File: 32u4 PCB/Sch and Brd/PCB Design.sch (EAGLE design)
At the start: 56 parts, among them J1 AVR_SPI_PROG_3X2PTH, J2 AMP FCI 10103594-0001LF, Q1 16MHz, U1 ATMEGA32U4-AU

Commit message: Started routinng
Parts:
- removed CONT: 50k, pot:TRIM_EU-S64W
- added I2C: (no value), pinhead:PINHD-1X4
- added R13: 220, resistor:R-EU_M0805
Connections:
- net +12V: no longer X1-2.KL
- net +5V: now also I2C.2; no longer CONT.E
- net GND: now also I2C.1, R13.1; no longer CONT.A, X1-1.KL
- net N$6: now also R13.2; no longer CONT.S
- net PD0/SCL: now also I2C.3
- net PD1/SDA: now also I2C.4
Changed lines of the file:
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@@
 <setting verticaltext="up"/>
 </settings>
-<grid distance="0.05" unitdist="inch" unit="inch" style="lines" multiple="1" display="no" altdistance="0.005" altunitdist="inch" altunit="inch"/>
+<grid distance="0.1" unitdist="inch" unit="inch" style="lines" multiple="1" display="no" altdistance="0.01" altunitdist="inch" altunit="inch"/>
 <layers>
 <layer number="1" name="Top" color="4" fill="1" visible="no" active="no"/>
@@
 </part>
 <part name="GND22" library="supply1" deviceset="GND" device=""/>
-<part name="CONT" library="pot" library_urn="urn:adsk.eagle:library:331" deviceset="TRIM_EU-" device="S64W" value="50k">
-<attribute name="MF" value=""/>
-<attribute name="MPN" value=""/>
-<attribute name="OC_FARNELL" value="unknown"/>
-</part>
-<part name="P+13" library="supply1" deviceset="+5V" device=""/>
-<part name="GND19" library="supply1" deviceset="GND" device=""/>
 <part name="P+12" library="supply1" deviceset="+5V" device=""/>
 <part name="LCD1" library="SparkFun-Displays" deviceset="LCD-16X2" device="NOSILK">
@@
 <part name="X1" library="con-ptr500" library_urn="urn:adsk.eagle:library:181" deviceset="AK500/2-H" device="" package3d_urn="urn:adsk.eagle:package:9901/1"/>
 <part name="MPU6040" library="pinhead" library_urn="urn:adsk.eagle:library:325" deviceset="PINHD-1X8" device="" package3d_urn="urn:adsk.eagle:package:22409/2"/>
+<part name="R13" library="resistor" library_urn="urn:adsk.eagle:library:348" deviceset="R-EU_" device="M0805" value="220">
+<attribute name="MF" value=""/>
+<attribute name="MPN" value=""/>
+<attribute name="OC_FARNELL" value="unknown"/>
+</part>
+<part name="GND3" library="supply1" deviceset="GND" device=""/>
+<part name="I2C" library="pinhead" library_urn="urn:adsk.eagle:library:325" deviceset="PINHD-1X4" device="" package3d_urn="urn:adsk.eagle:package:22407/2"/>
 </parts>
 <sheets>
@@
 <instance part="X1" gate="-2" x="3.81" y="144.78" rot="R180"/>
 <instance part="MPU6040" gate="A" x="139.7" y="-114.3"/>
+<instance part="I2C" gate="A" x="160.02" y="-66.04"/>
 </instances>
 <busses>
@@
 <wire x1="137.16" y1="-104.14" x2="132.08" y2="-104.14" width="0.1524" layer="91"/>
 <label x="132.08" y="-104.14" size="1.016" layer="95" rot="R180" xref="yes"/>
+</segment>
+<segment>
+<pinref part="I2C" gate="A" pin="2"/>
+<wire x1="157.48" y1="-63.5" x2="152.4" y2="-63.5" width="0.1524" layer="91"/>
+<label x="152.4" y="-63.5" size="1.016" layer="95" rot="R180" xref="yes"/>
 </segment>
 </net>
@@
 <wire x1="-12.7" y1="137.16" x2="-17.78" y2="137.16" width="0.1524" layer="91"/>
 <junction x="-17.78" y="137.16"/>
-<wire x1="-12.7" y1="137.16" x2="-1.27" y2="137.16" width="0.1524" layer="91"/>
-<junction x="-12.7" y="137.16"/>
-<pinref part="X1" gate="-1" pin="KL"/>
-<wire x1="-1.27" y1="138.43" x2="-1.27" y2="137.16" width="0.1524" layer="91"/>
 </segment>
 <segment>
@@
 <label x="132.08" y="-106.68" size="1.016" layer="95" rot="R180" xref="yes"/>
 </segment>
+<segment>
+<pinref part="I2C" gate="A" pin="1"/>
+<wire x1="157.48" y1="-60.96" x2="152.4" y2="-60.96" width="0.1524" layer="91"/>
+<label x="152.4" y="-60.96" size="1.016" layer="95" rot="R180" xref="yes"/>
+</segment>
 </net>
 <net name="PD1/SDA" class="0">
@@
 <wire x1="137.16" y1="-111.76" x2="132.08" y2="-111.76" width="0.1524" layer="91"/>
 <label x="132.08" y="-111.76" size="1.016" layer="95" rot="R180" xref="yes"/>
+</segment>
+<segment>
+<pinref part="I2C" gate="A" pin="4"/>
+<wire x1="157.48" y1="-68.58" x2="152.4" y2="-68.58" width="0.1524" layer="91"/>
+<label x="152.4" y="-68.58" size="1.016" layer="95" rot="R180" xref="yes"/>
 </segment>
 </net>
@@
 <junction x="-22.86" y="144.78"/>
 <pinref part="C1" gate="G$1" pin="+"/>
-<junction x="-12.7" y="144.78"/>
-<pinref part="X1" gate="-2" pin="KL"/>
-<wire x1="-1.27" y1="144.78" x2="-12.7" y2="144.78" width="0.1524" layer="91"/>
 </segment>
 </net>
@@
 <wire x1="137.16" y1="-109.22" x2="132.08" y2="-109.22" width="0.1524" layer="91"/>
 <label x="132.08" y="-109.22" size="1.016" layer="95" rot="R180" xref="yes"/>
+</segment>
+<segment>
+<pinref part="I2C" gate="A" pin="3"/>
+<wire x1="157.48" y1="-66.04" x2="152.4" y2="-66.04" width="0.1524" layer="91"/>
+<label x="152.4" y="-66.04" size="1.016" layer="95" rot="R180" xref="yes"/>
 </segment>
 </net>
@@
 </instance>
 <instance part="GND22" gate="1" x="22.86" y="15.24"/>
-<instance part="CONT" gate="1" x="-8.885290625" y="64.38225" smashed="yes">
-<attribute name="NAME" x="-14.854290625" y="60.57225" size="1.778" layer="95" rot="R90"/>
-<attribute name="VALUE" x="-12.695290625" y="60.57225" size="1.778" layer="96" rot="R90"/>
-<attribute name="OC_FARNELL" x="-8.885290625" y="64.38225" size="1.778" layer="96" display="off"/>
-<attribute name="MF" x="-8.885290625" y="64.38225" size="1.778" layer="96" display="off"/>
-<attribute name="MPN" x="-8.885290625" y="64.38225" size="1.778" layer="96" display="off"/>
-</instance>
-<instance part="P+13" gate="1" x="-10.16" y="73.66" smashed="yes">
-<attribute name="VALUE" x="-7.62" y="76.2" size="1.778" layer="96" rot="R180"/>
-</instance>
-<instance part="GND19" gate="1" x="-10.16" y="55.88"/>
 <instance part="P+12" gate="1" x="-5.08" y="33.02" smashed="yes" rot="R90">
 <attribute name="VALUE" x="0" y="35.56" size="1.778" layer="96" rot="R180"/>
@@
 <attribute name="MPN" x="35.56" y="48.26" size="1.778" layer="96" display="off"/>
 </instance>
+<instance part="R13" gate="G$1" x="-2.54" y="58.42" rot="R90">
+<attribute name="OC_FARNELL" x="-2.54" y="58.42" size="1.778" layer="96" display="off"/>
+<attribute name="MF" x="-2.54" y="58.42" size="1.778" layer="96" display="off"/>
+<attribute name="MPN" x="-2.54" y="58.42" size="1.778" layer="96" display="off"/>
+</instance>
+<instance part="GND3" gate="1" x="-2.54" y="48.26"/>
 </instances>
 <busses>
@@
 </segment>
 <segment>
-<pinref part="GND19" gate="1" pin="GND"/>
-<pinref part="CONT" gate="1" pin="A"/>
-<wire x1="-10.16" y1="58.42" x2="-8.885290625" y2="58.42" width="0.1524" layer="91"/>
-<wire x1="-8.885290625" y1="58.42" x2="-8.885290625" y2="59.30225" width="0.1524" layer="91"/>
+<pinref part="R13" gate="G$1" pin="1"/>
+<pinref part="GND3" gate="1" pin="GND"/>
+<wire x1="-2.54" y1="50.8" x2="-2.54" y2="53.34" width="0.1524" layer="91"/>
 </segment>
 </net>
@@
 <segment>
 <wire x1="25.4" y1="63.5" x2="-2.54" y2="63.5" width="0.1524" layer="91"/>
-<pinref part="CONT" gate="1" pin="S"/>
-<wire x1="-3.805290625" y1="64.38225" x2="-2.54" y2="64.38225" width="0.1524" layer="91"/>
-<wire x1="-2.54" y1="64.38225" x2="-2.54" y2="63.5" width="0.1524" layer="91"/>
 <pinref part="LCD1" gate="G$1" pin="VO"/>
+<pinref part="R13" gate="G$1" pin="2"/>
+<junction x="-2.54" y="63.5"/>
 </segment>
 </net>
@@
 </segment>
 <segment>
-<pinref part="P+13" gate="1" pin="+5V"/>
-<pinref part="CONT" gate="1" pin="E"/>
-<wire x1="-10.16" y1="71.12" x2="-8.885290625" y2="71.12" width="0.1524" layer="91"/>
-<wire x1="-8.885290625" y1="71.12" x2="-8.885290625" y2="69.46225" width="0.1524" layer="91"/>
-</segment>
-<segment>

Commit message: Rough layout ready
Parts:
- POWER: device pinhead:PINHD-2X3 -> pinhead:PINHD-2X4
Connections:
- net +5V: now also POWER.3, POWER.4
- net AREF: no longer POWER.3, POWER.4
- net GND: now also POWER.7, POWER.8
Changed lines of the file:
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@@
 <attribute name="OC_FARNELL" value="unknown"/>
 </part>
-<part name="POWER" library="pinhead" library_urn="urn:adsk.eagle:library:325" deviceset="PINHD-2X3" device="" package3d_urn="urn:adsk.eagle:package:22462/2">
+<part name="POWER" library="pinhead" library_urn="urn:adsk.eagle:library:325" deviceset="PINHD-2X4" device="" package3d_urn="urn:adsk.eagle:package:22461/2">
 <attribute name="MF" value=""/>
 <attribute name="MPN" value=""/>
@@
 <segment>
 <label x="124.46" y="2.54" size="1.27" layer="95" rot="R180" xref="yes"/>
-<pinref part="POWER" gate="A" pin="1"/>
+<pinref part="POWER" gate="A" pin="3"/>
 <wire x1="124.46" y1="2.54" x2="129.54" y2="2.54" width="0.1524" layer="91"/>
-<pinref part="POWER" gate="A" pin="2"/>
+<pinref part="POWER" gate="A" pin="4"/>
 <wire x1="129.54" y1="2.54" x2="137.16" y2="2.54" width="0.1524" layer="91"/>
 <junction x="129.54" y="2.54"/>
+<pinref part="POWER" gate="A" pin="1"/>
+<wire x1="129.54" y1="2.54" x2="129.54" y2="5.08" width="0.1524" layer="91"/>
+<pinref part="POWER" gate="A" pin="2"/>
+<wire x1="129.54" y1="5.08" x2="137.16" y2="5.08" width="0.1524" layer="91"/>
+<junction x="129.54" y="5.08"/>
 </segment>
 <segment>
@@
 <segment>
 <label x="124.46" y="-2.54" size="1.27" layer="95" rot="R180" xref="yes"/>
-<pinref part="POWER" gate="A" pin="5"/>
+<pinref part="POWER" gate="A" pin="7"/>
 <wire x1="124.46" y1="-2.54" x2="129.54" y2="-2.54" width="0.1524" layer="91"/>
-<pinref part="POWER" gate="A" pin="6"/>
+<pinref part="POWER" gate="A" pin="8"/>
 <wire x1="129.54" y1="-2.54" x2="137.16" y2="-2.54" width="0.1524" layer="91"/>
 <junction x="129.54" y="-2.54"/>
+<pinref part="POWER" gate="A" pin="6"/>
+<pinref part="POWER" gate="A" pin="5"/>
+<wire x1="137.16" y1="0" x2="129.54" y2="0" width="0.1524" layer="91"/>
+<wire x1="129.54" y1="0" x2="124.46" y2="0" width="0.1524" layer="91"/>
+<wire x1="124.46" y1="0" x2="124.46" y2="-2.54" width="0.1524" layer="91"/>
+<junction x="129.54" y="0"/>
 </segment>
 <segment>
@@
 </segment>
 <segment>
-<label x="123.19" y="0" size="1.27" layer="95" rot="R180" xref="yes"/>
-<pinref part="POWER" gate="A" pin="3"/>
-<wire x1="124.46" y1="0" x2="129.54" y2="0" width="0.1524" layer="91"/>
-<pinref part="POWER" gate="A" pin="4"/>
-<wire x1="129.54" y1="0" x2="137.16" y2="0" width="0.1524" layer="91"/>
-<junction x="129.54" y="0"/>
-</segment>
-<segment>

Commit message: Routing almost done
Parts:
- removed JP2, JP3, JP4, JP5: JUMPER-SMT_3_1-NC_PASTE_SILK, SparkFun-Jumpers:JUMPER-SMT_3_1-NC_PASTE_SILK
- LCD1: value LCD-16X2NOSILK -> LCD-16X2NOHOLES; device SparkFun-Displays:LCD-16X2NOSILK -> SparkFun-Displays:LCD-16X2NOHOLES
- R4, R5, R6, R8: value 1K -> 330
- renumbered PB1 to PE6, PB2 to PE2, PB5 to PC6
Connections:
- removed net CS: SPI_SD_CARD.1
- removed net D4: LCD1.DB4
- removed net D5: LCD1.DB5
- removed net D6: LCD1.DB6
- removed net D7: LCD1.DB7
- removed net E: LCD1.E
- removed net N$10: PE6.A
- removed net N$11: PE2.A
- removed net N$12: PC6.A
- removed net N$17: JP2.2, R11.1
- removed net N$18: BUTTON_1.P, BUTTON_1.P1, JP3.2
- removed net N$19: BUTTON_2.P, BUTTON_2.P1, JP5.2
- removed net N$20: JP4.2, R12.1
- removed net PB0: PORT_B.1, PORT_B.2, U1.PB0
- removed net RS: LCD1.RS
- new net PB0/SS: PORT_B.1, PORT_B.2, SPI_SD_CARD.1, U1.PB0
- net +5V: now also R11.1, R12.1; no longer JP2.1, JP3.3, JP4.1, JP5.3
- net GND: now also BUTTON_1.P, BUTTON_1.P1, BUTTON_2.P, BUTTON_2.P1; no longer JP2.3, JP3.1, JP4.3, JP5.1
- net PC6: now also PC6.A
- net PD0/SCL: now also I2C.4; no longer I2C.3
- net PD1/SDA: now also I2C.3; no longer I2C.4
- net PE2: now also PE2.A
- net PE6: now also PE6.A
- net PF0: now also LCD1.RS
- net PF1: now also LCD1.E
- net PF4/TCK: now also LCD1.DB4
- net PF5/TMS: now also LCD1.DB5
- net PF6/TDO: now also LCD1.DB6
- net PF7/TDI: now also LCD1.DB7

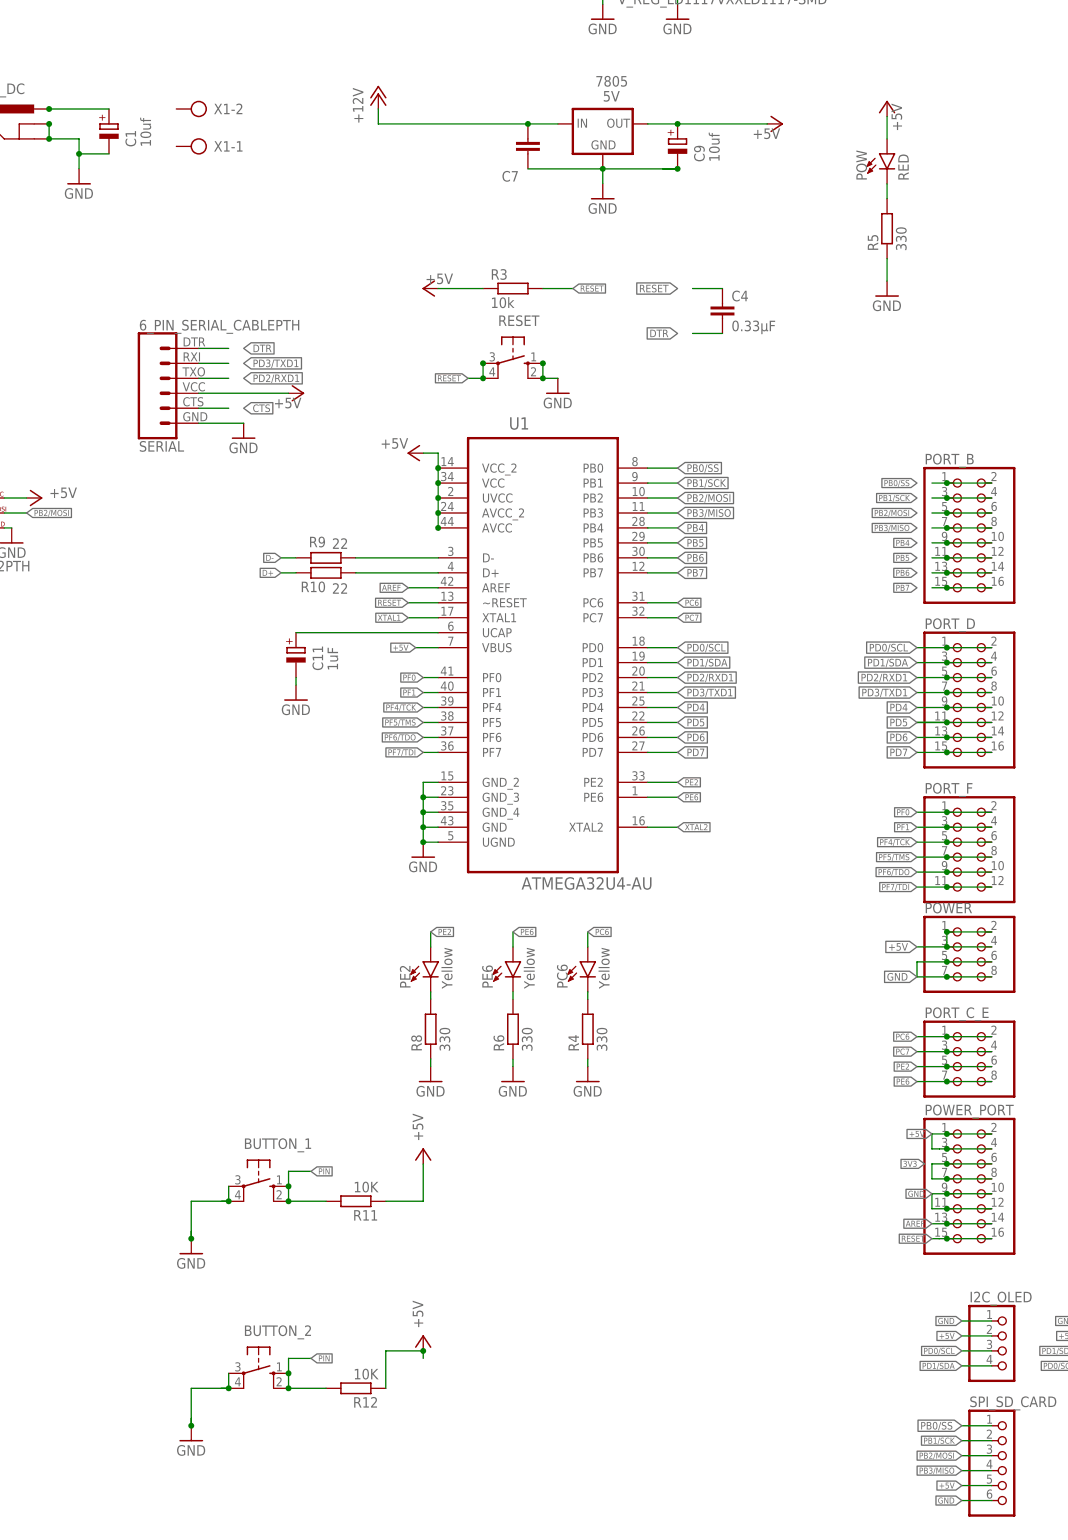
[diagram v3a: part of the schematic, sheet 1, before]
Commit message: Routing done - Awiiting verification
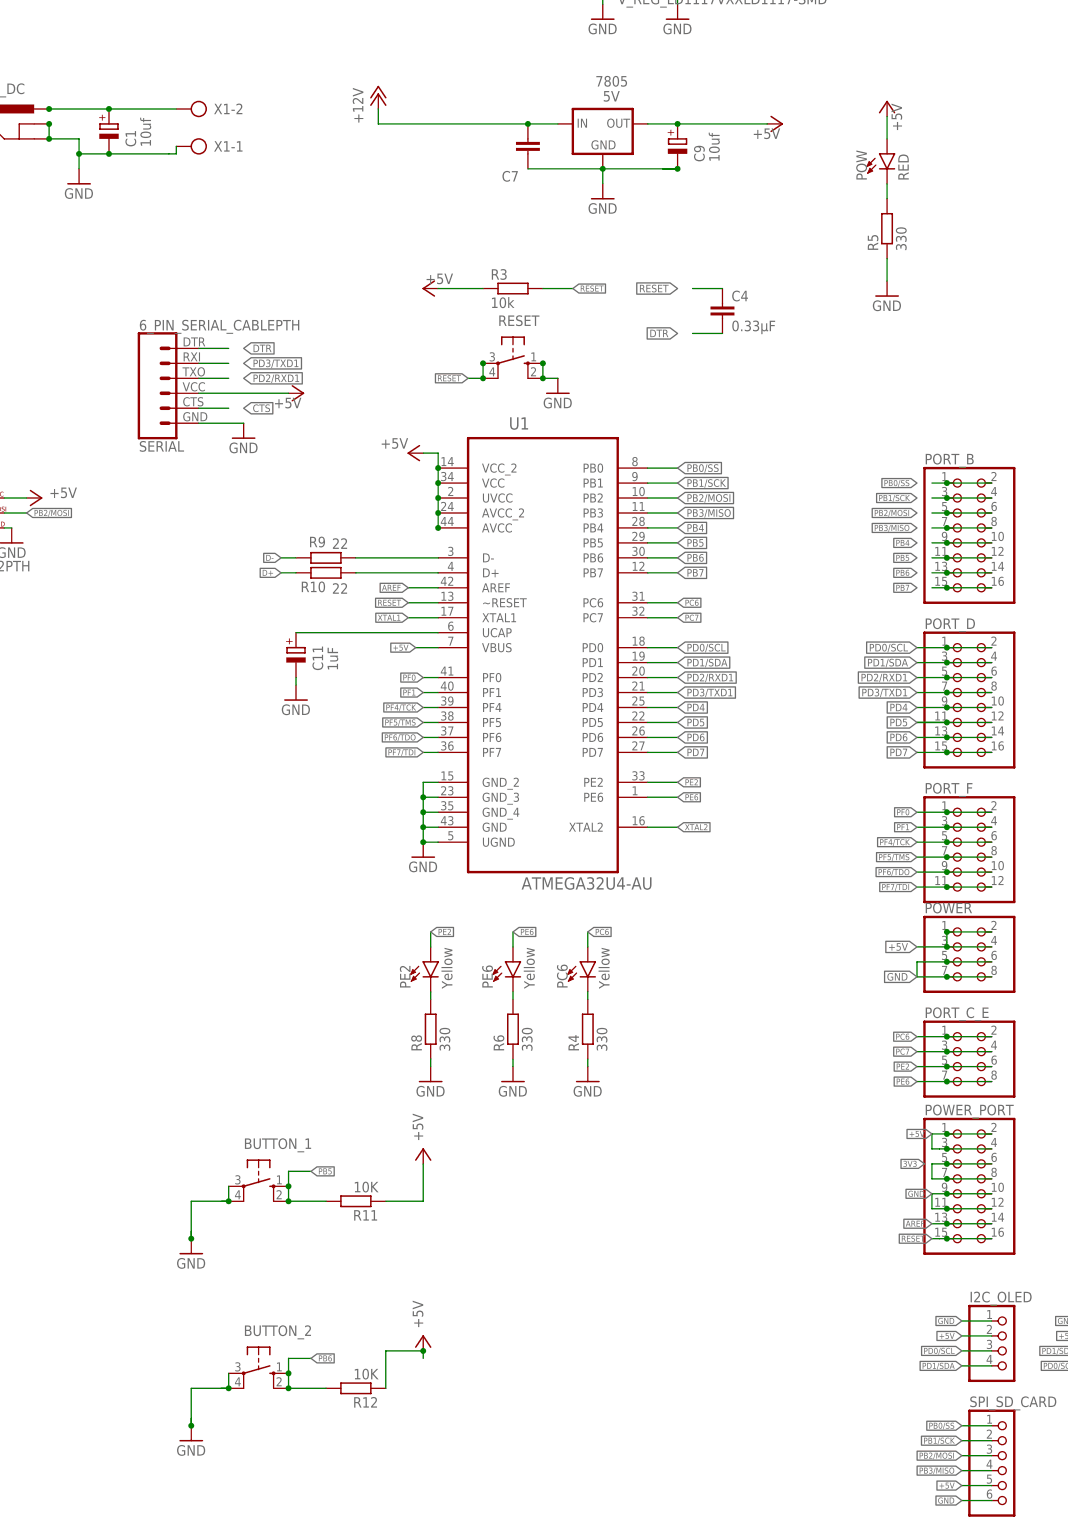
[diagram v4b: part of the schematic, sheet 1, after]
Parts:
- BUTTON_1, BUTTON_2, RESET: MF OMRON ELECTRONIC COMPONENTS -> OMRON
- I2C, I2C_OLED, J1, MPU6040, PORT_C_E, POWER_PORT, SPI_SD_CARD, U1: OC_FARNELL (none) -> unknown
- J2: MF (none) -> AMPHENOL ICC (FCI); MPN (none) -> 10103594-0001LF; OC_FARNELL (none) -> 2293752
- R13: value 220 -> 4k7
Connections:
- removed net 3.3V: 1117.OUT, C8.+
- removed net PIN: BUTTON_1.S, BUTTON_1.S1, BUTTON_2.S, BUTTON_2.S1, R11.2, R12.2
- net +12V: now also X1-2.KL
- net 3V3: now also 1117.OUT, C8.+
- net GND: now also X1-1.KL
- net PB5: now also BUTTON_1.S, BUTTON_1.S1, R11.2
- net PB6: now also BUTTON_2.S, BUTTON_2.S1, R12.2
